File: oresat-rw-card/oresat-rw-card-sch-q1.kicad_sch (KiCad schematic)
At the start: 76 parts, among them Q10 PMV45EN, Q5 DMP2240UDM, Q6 PMV45EN, Q7 DMP3050LVT-7, Q8 DMP3050LVT-7, U10 MAX4211FETE, U4 MAX7310, U7 MIC842LYC5, U8 MIC842LYC5, U9 TS5A21366DCUR

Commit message: Rename to oresat-rw-card, which is what this is.
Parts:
- removed C11, C12, C14, C16: 1u, oresat-passives:c_0603-SMALL, symbol Device:C_Small
- removed C13, C15: 100n, oresat-passives:c_0603-SMALL, symbol Device:C_Small
- removed C19: 10n, oresat-passives:c_0603-SMALL, symbol Device:C_Small
- removed C20: 470n, oresat-passives:c_0603-SMALL, symbol Device:C_Small
- removed D4: AMBER, oresat-acs-card:LED-0603, symbol Device:LED
- removed D6: GREEN, oresat-acs-card:LED-0603, symbol Device:LED
- removed Q10, Q6: PMV45EN, Package_TO_SOT_SMD:SOT-23, symbol Transistor_FET:Q_NMOS_GSD
- removed Q5: DMP2240UDM, Package_TO_SOT_SMD:SOT-23-6, symbol Transistor_FET:Q_Dual_PMOS_G1S2G2D2S1D1
- removed Q7, Q8: DMP3050LVT-7, Package_TO_SOT_SMD:TSOT-23-6, symbol oresat-transistors:DMP3050LVT-7
- removed R43, R44, R45, R46, R47, R48, R51, R52, R53, R54, R55, R56, R57, R60, R61, R71, R72: 100, Resistor_SMD:R_0603_1608Metric, symbol Device:R_Small_US
- removed R58, R59: 665k, Resistor_SMD:R_0603_1608Metric, symbol Device:R_Small_US
- removed R62, R67, R68, R70, R74, R78, R83, R84, R86, R88: 10k, Resistor_SMD:R_0603_1608Metric, symbol Device:R_Small_US
- removed R63, R64: 330k, Resistor_SMD:R_0603_1608Metric, symbol Device:R_Small_US
- removed R65, R66: 1M, Resistor_SMD:R_0603_1608Metric, symbol Device:R_Small_US
- removed R69: 4.7k, Resistor_SMD:R_0603_1608Metric, symbol Device:R_Small_US
- removed R73: 100k, Resistor_SMD:R_0603_1608Metric, symbol Device:R_Small_US
- removed R75: 15m, oresat-acs-card:R1206, symbol Device:R_Small_US
- removed R79, R80, R81, R82: 0, Resistor_SMD:R_0603_1608Metric, symbol Device:R_Small_US
- removed R85: 10k, oresat-passives:0603-C-NOSILK, symbol Device:R_US
- removed TP20, TP21, TP22, TP23, TP24, TP25, TP26, TP27, TP28, TP29, TP31, TP32, TP33, TP36, TP37: Test-Point, oresat-misc:TestPoint-0.75mm-th, symbol oresat-misc:Test-Point-0.75mm-th
- removed U10: MAX4211FETE, Package_DFN_QFN:QFN-16-1EP_4x4mm_P0.65mm_EP2.1x2.1mm, symbol oresat-ics:MAX4211D/E/F
- removed U4: MAX7310, Package_DFN_QFN:QFN-16-1EP_4x4mm_P0.65mm_EP2.1x2.1mm, symbol oresat-ics:MAX7310
- removed U7, U8: MIC842LYC5, Package_TO_SOT_SMD:SOT-353_SC-70-5, symbol oresat-ics:MIC842LYC5
- removed U9: TS5A21366DCUR, Package_SO:VSSOP-8_2.3x2mm_P0.5mm, symbol oresat-ics:TS5A21366
- added C2, C3, C6, C7: 1u, oresat-passives:c_0603-SMALL, symbol Device:C_Small
- added C4, C5: 100n, oresat-passives:c_0603-SMALL, symbol Device:C_Small
- added C68: 10n, oresat-passives:c_0603-SMALL, symbol Device:C_Small
- added C69: 470n, oresat-passives:c_0603-SMALL, symbol Device:C_Small
- added D1: AMBER, oresat-acs-card:LED-0603, symbol Device:LED
- added D2: GREEN, oresat-acs-card:LED-0603, symbol Device:LED
- added Q1: DMP2240UDM, Package_TO_SOT_SMD:SOT-23-6, symbol Transistor_FET:Q_Dual_PMOS_G1S2G2D2S1D1
- added Q2, Q9: PMV45EN, Package_TO_SOT_SMD:SOT-23, symbol Transistor_FET:Q_NMOS_GSD
- added Q3, Q4: DMP3050LVT-7, Package_TO_SOT_SMD:TSOT-23-6, symbol oresat-transistors:DMP3050LVT-7
- added R1, R10, R11, R12, R13, R16, R17, R2, R24, R25, R3, R4, R5, R6, R7, R8, R9: 100, Resistor_SMD:R_0603_1608Metric, symbol Device:R_Small_US
- added R14, R15: 665k, Resistor_SMD:R_0603_1608Metric, symbol Device:R_Small_US
- added R18, R23, R26, R28, R30, R32, R37, R38, R41, R49: 10k, Resistor_SMD:R_0603_1608Metric, symbol Device:R_Small_US
- added R19, R20: 330k, Resistor_SMD:R_0603_1608Metric, symbol Device:R_Small_US
- added R21, R22: 1M, Resistor_SMD:R_0603_1608Metric, symbol Device:R_Small_US
- added R27: 4.7k, Resistor_SMD:R_0603_1608Metric, symbol Device:R_Small_US
- added R29: 100k, Resistor_SMD:R_0603_1608Metric, symbol Device:R_Small_US
- added R31: 15m, oresat-acs-card:R1206, symbol Device:R_Small_US
- added R33, R34, R35, R36: 0, Resistor_SMD:R_0603_1608Metric, symbol Device:R_Small_US
- added R50: 10k, oresat-passives:0603-C-NOSILK, symbol Device:R_US
- added TP10, TP11, TP12, TP13, TP14, TP15, TP17, TP2, TP3, TP4, TP5, TP6, TP7, TP8, TP9: Test-Point, oresat-misc:TestPoint-0.75mm-th, symbol oresat-misc:Test-Point-0.75mm-th
- added U1: MAX7310, Package_DFN_QFN:QFN-16-1EP_4x4mm_P0.65mm_EP2.1x2.1mm, symbol oresat-ics:MAX7310
- added U18: MAX4211FETE, Package_DFN_QFN:QFN-16-1EP_4x4mm_P0.65mm_EP2.1x2.1mm, symbol oresat-ics:MAX4211D/E/F
- added U2, U3: MIC842LYC5, Package_TO_SOT_SMD:SOT-353_SC-70-5, symbol oresat-ics:MIC842LYC5
- added U5: TS5A21366DCUR, Package_SO:VSSOP-8_2.3x2mm_P0.5mm, symbol oresat-ics:TS5A21366
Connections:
- net AD0: now also R12.1, R13.2, R16.1, R17.2, U1.1 (AD0)
- net AD1: now also R10.1, R11.2, R8.1, R9.2, U1.2 (AD1)
- net AD2: now also R2.1, R3.2, R4.1, R5.2, U1.3 (AD2)
- net C3-UART-RX: now also R24.1
- net C3-UART-TX: now also R25.1
- net CB-RESET: now also R32.2, TP13.1, U1.9 (IO4), U18.9 (CIN2-)
- net CB_CTRL: now also Q9.1 (G), R49.1, TP10.1, U18.3 (LE), U18.4 (COUT1), U18.6 (COUT2)
- net GND: now also C2.2, C3.2, C4.2, C5.2, C6.2, D1.1 (K), D2.1 (K), Q2.2 (S), Q9.2 (S), R11.1, R17.1, R23.1, R26.2, R29.2, R32.1, R35.2, R36.2, R5.1, U1.17 (GND), U1.6 (GND), U18.17 (GND), U18.7 (GND), U2.2 (GND), U3.2 (GND), U5.4 (GND)
- net ON/~{OFF}: now also C5.1, C6.1, Q2.1 (G), R26.1, R27.2, TP9.1, U1.8 (IO3), U18.1 (VCC), U18.2 (IN), U5.8 (Vcc)
- net OPD_PWR: now also R1.2
- net OPD_SCL: now also R6.2
- net OPD_SDA: now also R7.2
- net PEN-SCL-FILT: now also Q1.4 (D), R12.2, R19.2, R2.2, R8.2, TP3.1, U1.15 (SCL)
- net PEN-SDA-FILT: now also Q1.6 (D), R10.2, R16.2, R20.2, R4.2, TP4.1, U1.16 (SDA)
- net POUT: now also TP11.1, U18.13 (POUT)
- net UART_EN: now also R23.2, TP5.1, U1.12 (IO7), U5.3 (IN2), U5.7 (IN1)
- net VBUS: now also Q3.4 (S), R28.1
- net VPD: now also C4.1, R1.1, R13.1, R18.2, R21.2, R22.2, R3.1, R38.2, R9.1, TP2.1, U1.14 (V+), U2.5 (VDD), U3.5 (VDD)
- net ~{FAULT}: now also Q9.3 (D), R38.1, TP15.1, U1.7 (IO2)
- new net: C68.1, Q4.4 (S), R31.2, R37.2, U18.15 (RS-)
- new net: C68.2, Q4.3 (G), R37.1, R49.2, R50.2
- new net: Q1.1 (G), R15.2
- new net: Q1.5 (S), R7.1
- new net: C2.1, R19.1, R21.1, U2.1 (INP)
- new net: D2.2 (A), R41.1
- new net: C69.2, R50.1
- new net: Q2.3 (D), Q3.3 (G), R28.2
- new net: C7.2, R29.1, R30.2
- new net: TP6.1, U1.11 (IO6)
- new net: R18.1, U1.13 (~{RESET})
- new net: R24.2, U5.1 (NO1)
- new net: R25.2, U5.5 (NO2)
- new net: R30.1, U18.5 (INHIBIT)
- new net: C3.1, R20.1, R22.1, U3.1 (INP)
- new net: R34.1, R36.1, TP14.1, U18.10 (CIN1+)
- new net: R34.2, U18.14 (IOUT)
- new net: R15.1, TP8.1, U3.4 (OUT)
- new net: D1.2 (A), R27.1
- new net: R14.1, TP7.1, U2.4 (OUT)
- new net: Q1.3 (G), R14.2
- new net: Q1.2 (S), R6.1
- new net: R33.1, R35.1, TP12.1, U18.11 (CIN1-)
- new net: R33.2, U18.12 (REF), U18.8 (CIN2+)
- new net: Q3.1 (D), Q3.2 (D), Q3.5 (D), Q3.6 (D), R31.1, U18.16 (RS+)
- new net BOOTCFG-Q1: U1.10 (IO5)
- new net RW-UART-RX-Q1: U5.6 (COM2)
- new net RW-UART-TX-Q1: U5.2 (COM1)
- new net VBUSP-Q1: C69.1, C7.1, Q4.1 (D), Q4.2 (D), Q4.5 (D), Q4.6 (D), R41.2, TP17.1
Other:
- note removed: "To MCXN digitally configued boot pin"

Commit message: Cleaned up Q1, added notes for other sheets.
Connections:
- net VPD renamed VPD-Q1
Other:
- note removed: "(3.3V)"
- note removed: "Card Power Switch and Circuit Breaker"
- note removed: "Note: Address 0b0111110x is reserved on all oresat cards"
- note removed: "OreSat Power Domain (OPD) Controller"
- moved on the sheet: C2, C3, C4, C5, C6, C68, C69, C7, D1, D2, Q1A, Q1B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

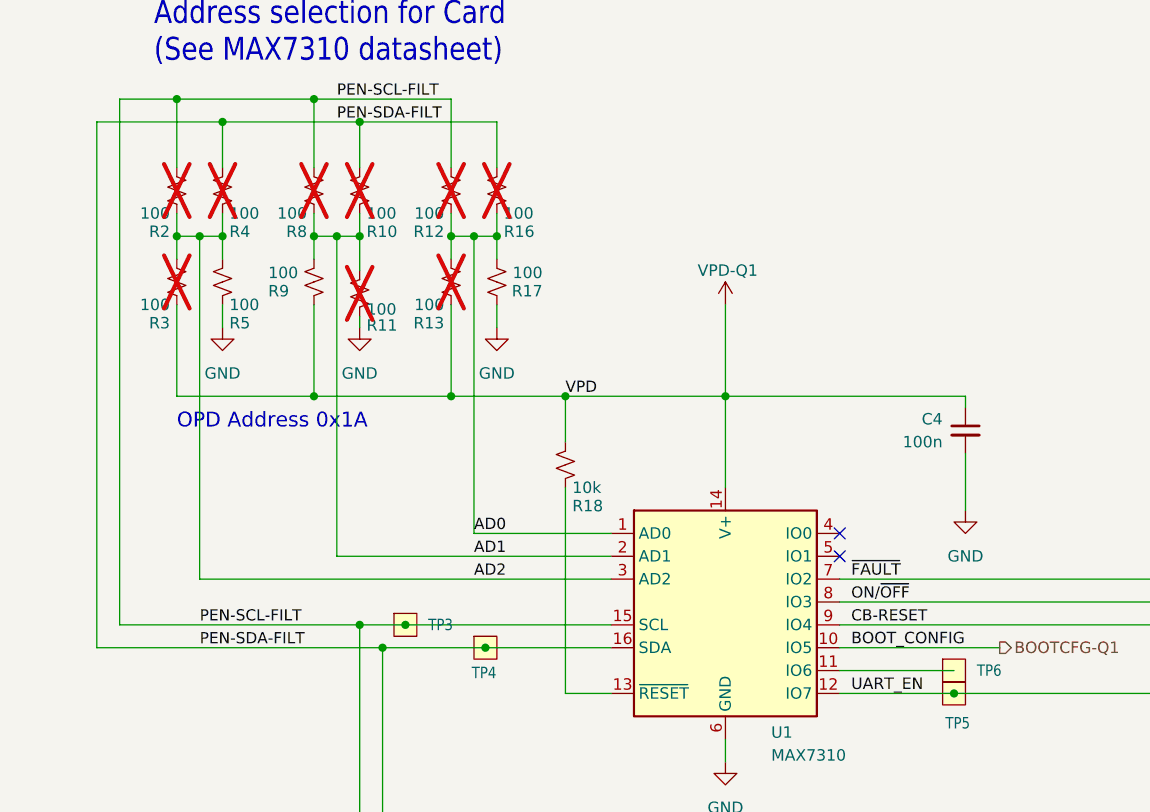
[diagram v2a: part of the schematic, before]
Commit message: Schematic Done + Board outline set
Fixed heirarchical labels, cleaned up ERCs, board is ready for layout
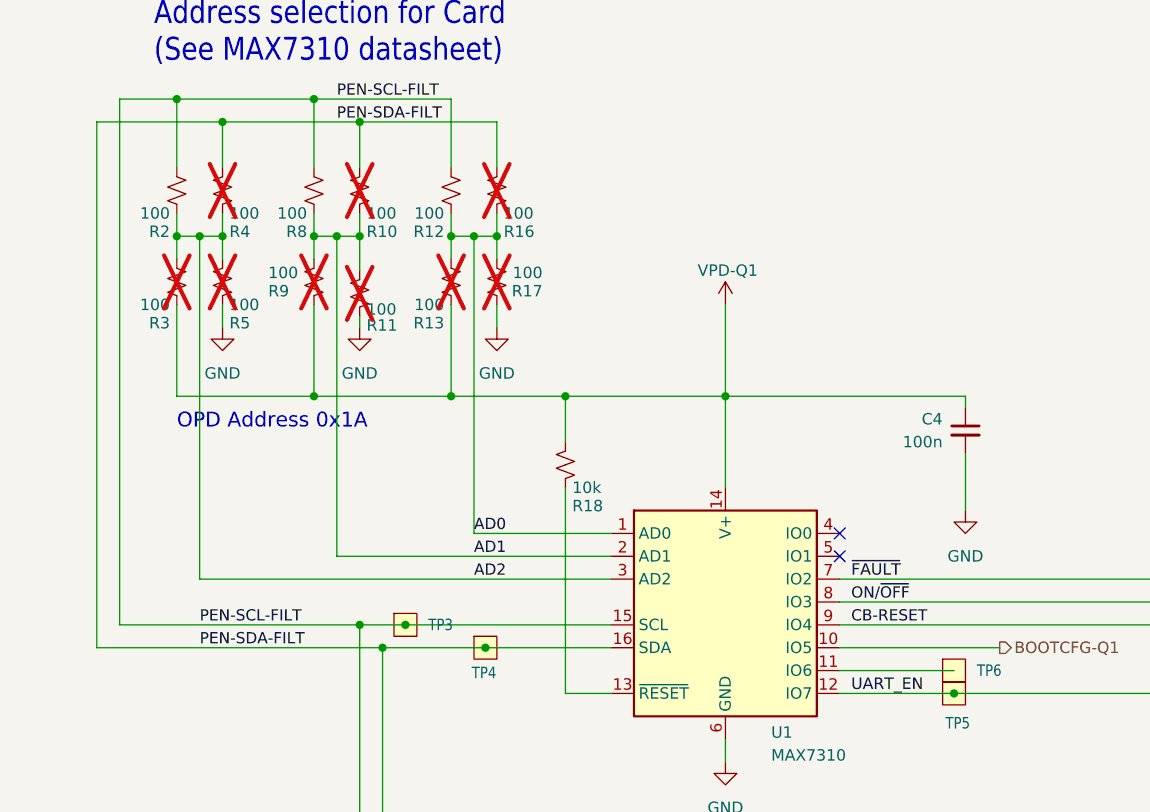
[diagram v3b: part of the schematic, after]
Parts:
- C2, C3, C4, C5, C6, C68, C69, C7: footprint oresat-passives:c_0603-SMALL -> Capacitor_SMD:C_0201_0603Metric
- R12, R2, R8: now fitted
- R17, R5, R9: now not fitted

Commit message: Lots of work needs to be done still
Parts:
- C2, C3, C4, C5, C6, C68, C69, C7: footprint Capacitor_SMD:C_0201_0603Metric -> Capacitor_SMD:C_0603_1608Metric
- D1: footprint oresat-acs-card:LED-0603 -> LED_SMD:LED_0603_1608Metric_Pad1.05x0.95mm_HandSolder
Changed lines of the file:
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@@
 			)
 		)
-		(property "Footprint" "Capacitor_SMD:C_0201_0603Metric"
+		(property "Footprint" "Capacitor_SMD:C_0603_1608Metric"
 			(at 349.25 44.45 0)
 			(effects
@@
 			)
 		)
-		(property "Footprint" "Capacitor_SMD:C_0201_0603Metric"
+		(property "Footprint" "Capacitor_SMD:C_0603_1608Metric"
 			(at 242.57 57.15 0)
 			(effects
@@
 			)
 		)
-		(property "Footprint" "Capacitor_SMD:C_0201_0603Metric"
+		(property "Footprint" "Capacitor_SMD:C_0603_1608Metric"
 			(at 92.71 184.15 0)
 			(effects
@@
 			)
 		)
-		(property "Footprint" "Capacitor_SMD:C_0201_0603Metric"
+		(property "Footprint" "Capacitor_SMD:C_0603_1608Metric"
 			(at 92.71 228.6 0)
 			(effects
@@
 			)
 		)
-		(property "Footprint" "Capacitor_SMD:C_0201_0603Metric"
+		(property "Footprint" "Capacitor_SMD:C_0603_1608Metric"
 			(at 234.95 135.89 0)
 			(effects
@@
 			)
 		)
-		(property "Footprint" "oresat-acs-card:LED-0603"
+		(property "Footprint" "LED_SMD:LED_0603_1608Metric_Pad1.05x0.95mm_HandSolder"
 			(at 196.85 85.09 0)
 			(effects
@@
 			)
 		)
-		(property "Footprint" "Capacitor_SMD:C_0201_0603Metric"
+		(property "Footprint" "Capacitor_SMD:C_0603_1608Metric"
 			(at 132.08 106.68 0)
 			(effects
@@
 			)
 		)
-		(property "Footprint" "Capacitor_SMD:C_0201_0603Metric"
+		(property "Footprint" "Capacitor_SMD:C_0603_1608Metric"
 			(at 232.41 58.42 0)
 			(effects
@@
 			)
 		)
-		(property "Footprint" "Capacitor_SMD:C_0201_0603Metric"
+		(property "Footprint" "Capacitor_SMD:C_0603_1608Metric"
 			(at 373.38 44.45 0)
 			(effects

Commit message: Push for design review
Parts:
- added C8, C9: 100n, Capacitor_SMD:C_0603_1608Metric, symbol Device:C_Small
- D2: footprint oresat-acs-card:LED-0603 -> LED_SMD:LED_0603_1608Metric_Pad1.05x0.95mm_HandSolder
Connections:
- net GND: now also C8.2, C9.2
- net VPD-Q1: now also C8.1, C9.1

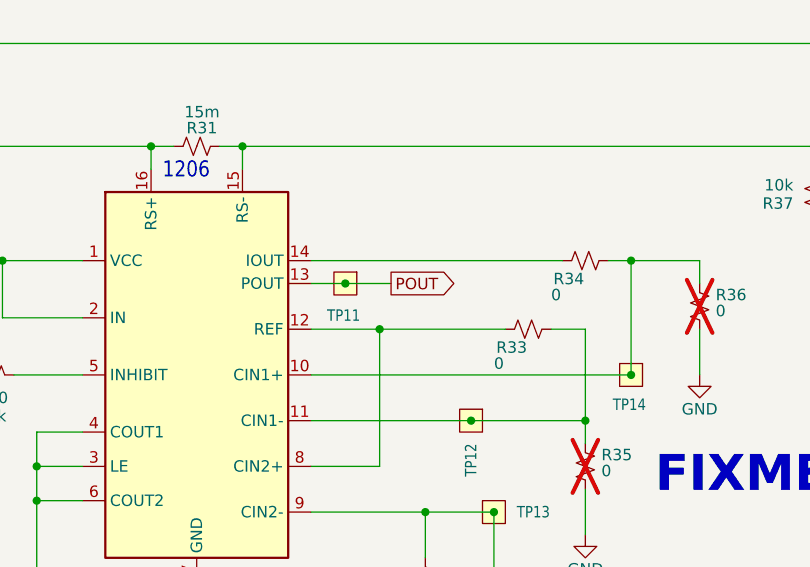
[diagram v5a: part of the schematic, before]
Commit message: Another try of the Q1 layout. 3/4 good, but not good for all 4 quadrants
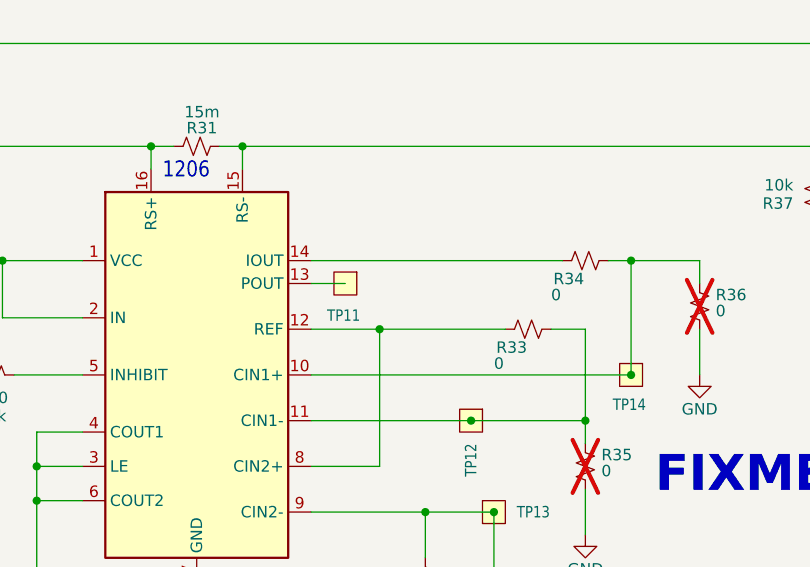
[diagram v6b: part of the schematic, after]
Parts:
- C2, C3, C4, C5, C6, C68, C69, C7, C8, C9: footprint Capacitor_SMD:C_0603_1608Metric -> oresat-passives:0603-C-NOSILK
- R1, R10, R11, R12, R13, R14, R15, R16, R17, R18, R19, R2, R20, R21, R22, R23, R24, R25, R26, R27, R28, R29, R3, R30, R32, R33, R34, R35, R36, R37, R38, R4, R41, R49, R5, R6, R7, R8, R9: footprint Resistor_SMD:R_0603_1608Metric -> oresat-passives:0603-C-NOSILK
- R31: footprint oresat-acs-card:R1206 -> oresat-passives:1206-C
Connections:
- net POUT: no longer names the net of TP11.1, U18.13 (POUT)

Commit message: Design review on current state of sch/brd
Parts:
- R1, R12, R2, R24, R25, R6, R7, R8: DIS (none) -> DigiKey; DPN (none) -> RMCF0603FT100RCT-ND; MFR (none) -> Stackpole Electronics; MPN (none) -> RMCF0603FT100R
- R14, R15: DIS (none) -> DigiKey; DPN (none) -> RMCF0603FT665KCT-ND; MFR (none) -> Stackpole Electronics; MPN (none) -> RMCF0603FT665K
